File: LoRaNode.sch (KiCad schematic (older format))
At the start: 60 parts, among them J1 CONN_01X04, J10 D4, J11 A1, J12 A2, J13 A3, J14 D8, J2 Conn_01x06, J3 Conn_01x02, J4 ISP, J5 Conn_01x06, J6 Conn_01x04, J7 USB_B_Micro, J8 D2, J9 D3, U1 RFM95W-868S2, U2 MCP73871, U3 TPS63031, U4 ATMEGA328P-AU, Y1 8MHz HC5032/4

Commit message: v0.1
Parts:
- removed C10, C4, C5, C6, C7, C9: 10u, Capacitors_SMD:C_0805, symbol device:C
- removed C3: 4700uF/10V, Capacitors_THT:CP_Radial_D12.5mm_P25mm, symbol device:CP
- removed C8: 100n, Capacitors_SMD:C_0603, symbol device:C
- removed D1: MBR120VLSFT1G, Capacitors_SMD:C_0805, symbol device:D
- removed D2: CHRG, LEDs:LED_0805, symbol device:LED
- removed D3: DONE, LEDs:LED_0805, symbol device:LED
- removed D4: PWR, LEDs:LED_0805, symbol device:LED
- removed J1: CONN_01X04, Mlab_CON:RJ12GLP-AMP(RJ12), symbol LoRaNode-rescue:CONN_01X04-RESCUE-Arduino_Mini-Arduino_Mini-rescue
- removed J2: Conn_01x06, Pin_Headers:Pin_Header_Straight_1x06_Pitch2.54mm, symbol Connector:Conn_01x06
- removed J3: Conn_01x02, Pin_Headers:Pin_Header_Straight_1x02_Pitch2.54mm, symbol Connector:Conn_01x02
- removed J7: USB_B_Micro, Connector_USB:USB_Micro-B_Molex-105017-0001, symbol Connector:USB_B_Micro
- removed L2: 1u5, Inductors:Inductor_Wurth_MAPI-3012, symbol device:L
- removed R1, R2, R3: 1k, Resistors_SMD:R_0603, symbol device:R
- removed R10: 69k8, Resistors_SMD:R_0603, symbol device:R
- removed R4: 270k, Resistors_SMD:R_0603, symbol device:R
- removed R5, R7: 100k, Resistors_SMD:R_0603, symbol device:R
- removed R6: 2k, Resistors_SMD:R_0603, symbol device:R
- removed R8: 1k54, Resistors_SMD:R_0603, symbol device:R
- removed R9: THERM 10k, Resistors_SMD:R_0805, symbol device:R
- removed U2: MCP73871, Housings_DFN_QFN:QFN-20-1EP_4x4mm_Pitch0.5mm, symbol MLAB_IO:MCP73871
- removed U3: TPS63031, Package_SON:Texas_S-PWSON-N10, symbol MLAB_IO:TPS63031
- added J1: A3, TestPoint:TestPoint_Pad_D1.0mm, symbol Connector:Conn_01x01
- added J2: Conn_01x03, Connector_PinHeader_2.54mm:PinHeader_1x03_P2.54mm_Vertical, symbol Connector:Conn_01x03
- C1: value 2p7 -> dnp
- L1: value 1n8 -> 0R
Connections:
- net labels added: GND
- net labels removed: A4, A5, Earth, VOUT, VSOL
- wire segments 223 -> 110
- no-connect marks 9 -> 6
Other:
- note added: "LoRa Node"
- note removed: "Charge Rate = 1000V/PROG1\n1k = 1000 mA\n2k = 500 mA"
- note removed: "No Thermistor: RT1 = 0R, RT2 = 10k\n10k NTC Thermistor: RT1 = 1k54, RT2 = 69k8"
- note removed: "ToDo:\nChange ground symbols\n"
- moved on the sheet: C1, C11, C12, C13, C14, C15, C16, C17, C18, C19, C2, C20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

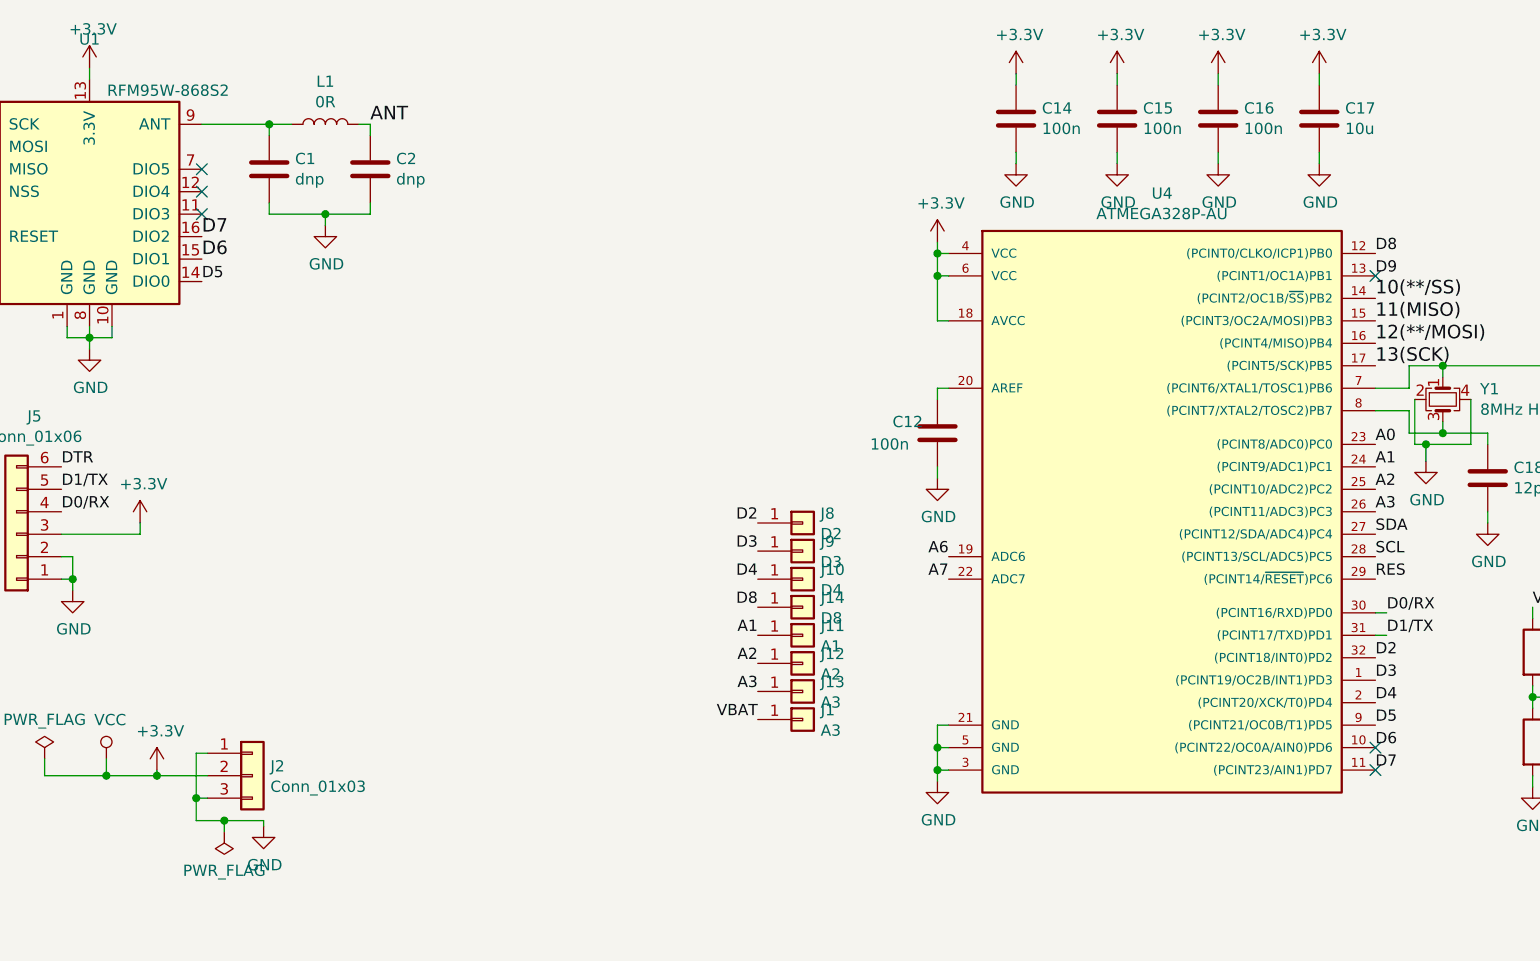
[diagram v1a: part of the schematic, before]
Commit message: Moved I2C and Power connectors, Added antenna test pads, ERC done, DRC done
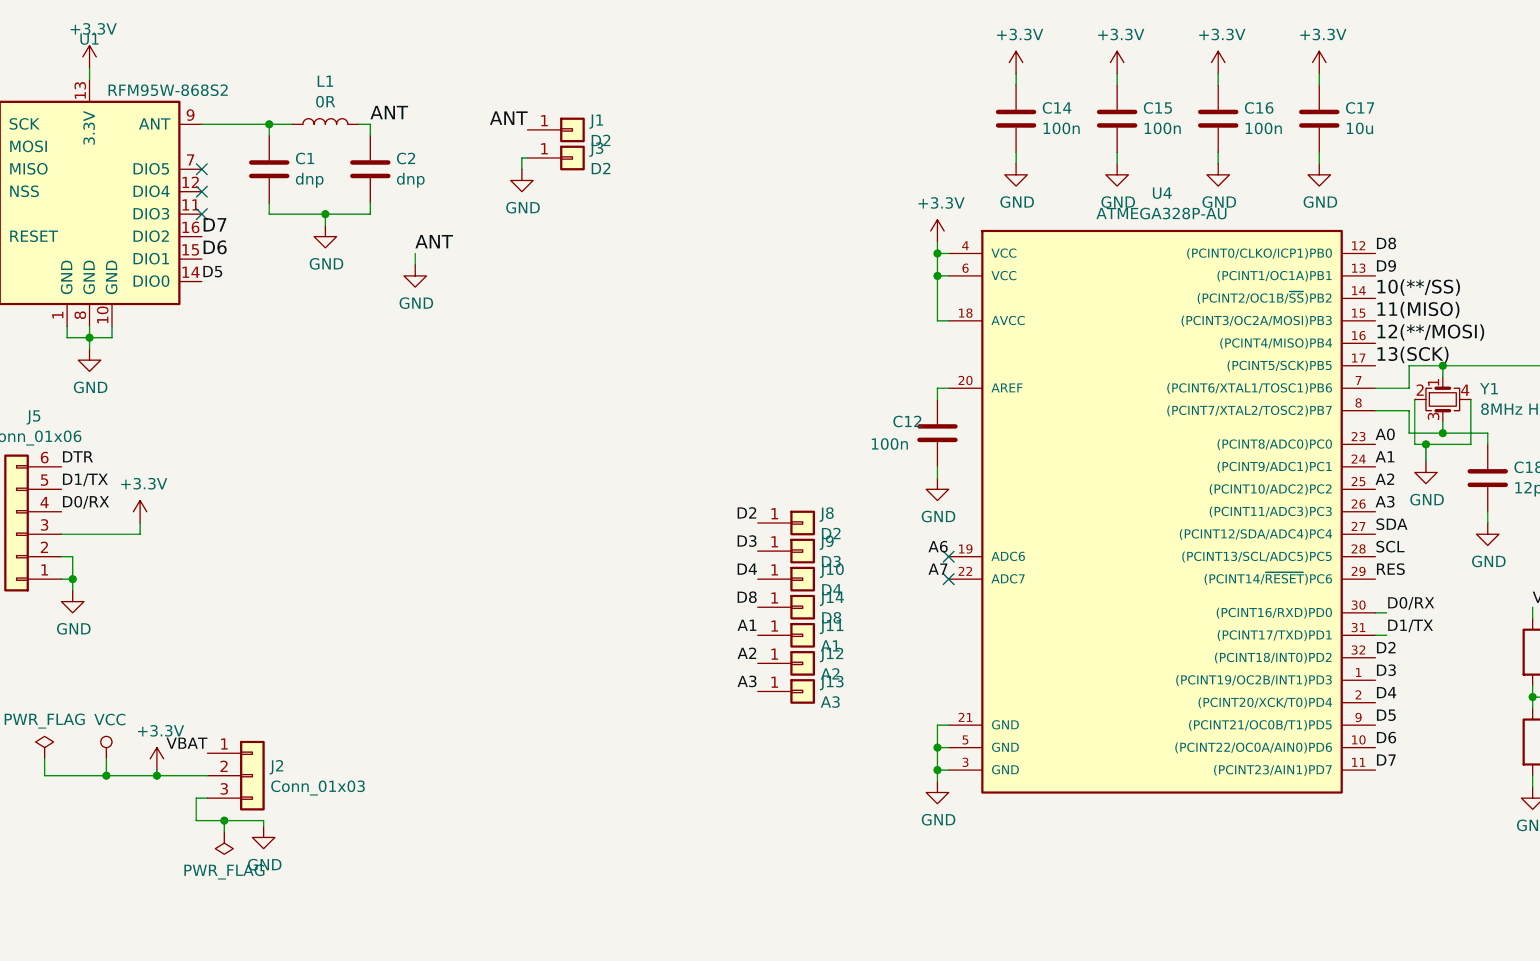
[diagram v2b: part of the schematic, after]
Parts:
- added J3: D2, TestPoint:TestPoint_Pad_1.0x1.0mm, symbol Connector:Conn_01x01
- J1: value A3 -> D2; footprint TestPoint:TestPoint_Pad_D1.0mm -> TestPoint:TestPoint_Pad_2.0x2.0mm
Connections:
- wire segments 110 -> 111
- no-connect marks 6 -> 5
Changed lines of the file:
@@
 Text Label 3775 3100 0    50   ~ 0
 D5
-NoConn ~ 9000 5175
-NoConn ~ 9000 5275
-NoConn ~ 9000 3075
 $Comp
 L device:R R16
@@
 	4050 5500 4050 5525
 Wire Wire Line
-	3800 5200 3750 5200
-Wire Wire Line
-	3750 5200 3750 5400
-Wire Wire Line
 	3750 5500 3875 5500
 Wire Wire Line
 	3800 5400 3750 5400
-Connection ~ 3750 5400
 Wire Wire Line
 	3750 5400 3750 5500
@@
 	1    0    0    -1
 $EndComp
+Text Label 3800 5200 2    50   ~ 0
+VBAT
 $Comp
 L Connector:Conn_01x01 J1
-U 1 1 5C90461F
-P 6450 5050
-F 0 "J1" H 6530 5092 50  0000 L CNN
-F 1 "A3" H 6530 5001 50  0000 L CNN
-F 2 "TestPoint:TestPoint_Pad_D1.0mm" H 6450 5050 50  0001 C CNN
-F 3 "~" H 6450 5050 50  0001 C CNN
-	1    6450 5050
-	1    0    0    -1
-$EndComp
-Text Label 6250 5050 2    50   ~ 0
-VBAT
+U 1 1 5C94DB3B
+P 5425 2425
+F 0 "J1" H 5504 2467 50  0000 L CNN
+F 1 "D2" H 5504 2376 50  0000 L CNN
+F 2 "TestPoint:TestPoint_Pad_2.0x2.0mm" H 5425 2425 50  0001 C CNN
+F 3 "~" H 5425 2425 50  0001 C CNN
+	1    5425 2425
+	1    0    0    -1
+$EndComp
+Text Label 5225 2425 2    60   ~ 0
+ANT
+$Comp
+L Connector:Conn_01x01 J3
+U 1 1 5C9511AC
+P 5425 2550
+F 0 "J3" H 5504 2592 50  0000 L CNN
+F 1 "D2" H 5504 2501 50  0000 L CNN
+F 2 "TestPoint:TestPoint_Pad_1.0x1.0mm" H 5425 2550 50  0001 C CNN
+F 3 "~" H 5425 2550 50  0001 C CNN
+	1    5425 2550
+	1    0    0    -1
+$EndComp
+$Comp
+L power:GND #PWR0121
+U 1 1 5C95121C
+P 5200 2600
+F 0 "#PWR0121" H 5200 2350 50  0001 C CNN
+F 1 "GND" H 5205 2427 50  0000 C CNN
+F 2 "" H 5200 2600 50  0001 C CNN
+F 3 "" H 5200 2600 50  0001 C CNN
+	1    5200 2600
+	1    0    0    -1
+$EndComp
+Wire Wire Line
+	5225 2550 5200 2550
+Wire Wire Line
+	5200 2550 5200 2600
+NoConn ~ 7100 4325
+NoConn ~ 7100 4425
+Text Label 4725 2975 0    60   ~ 0
+ANT
+$Comp
+L power:GND #PWR0122
+U 1 1 5C95F96A
+P 4725 3025
+F 0 "#PWR0122" H 4725 2775 50  0001 C CNN
+F 1 "GND" H 4730 2852 50  0000 C CNN
+F 2 "" H 4725 3025 50  0001 C CNN
+F 3 "" H 4725 3025 50  0001 C CNN
+	1    4725 3025
+	1    0    0    -1
+$EndComp
+Wire Wire Line
+	4725 2975 4725 3025
 $EndSCHEMATC

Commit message: Changed I2C pinout
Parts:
- added J7: A3, TestPoint:TestPoint_Pad_D1.0mm, symbol Connector:Conn_01x01
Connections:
- no-connect marks 5 -> 4
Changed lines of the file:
@@
 	-1   0    0    1
 $EndComp
+Text Label 1875 5450 0    50   ~ 0
+SDA
 Text Label 1875 5350 0    50   ~ 0
-SDA
-Text Label 1875 5450 0    50   ~ 0
 SCL
 $Comp
@@
 	5200 2550 5200 2600
 NoConn ~ 7100 4325
-NoConn ~ 7100 4425
 Text Label 4725 2975 0    60   ~ 0
 ANT
@@
 Wire Wire Line
 	4725 2975 4725 3025
+$Comp
+L Connector:Conn_01x01 J7
+U 1 1 5C9520C6
+P 6450 5050
+F 0 "J7" H 6530 5092 50  0000 L CNN
+F 1 "A3" H 6530 5001 50  0000 L CNN
+F 2 "TestPoint:TestPoint_Pad_D1.0mm" H 6450 5050 50  0001 C CNN
+F 3 "~" H 6450 5050 50  0001 C CNN
+	1    6450 5050
+	1    0    0    -1
+$EndComp
+Text Label 6250 5050 2    50   ~ 0
+A7
 $EndSCHEMATC

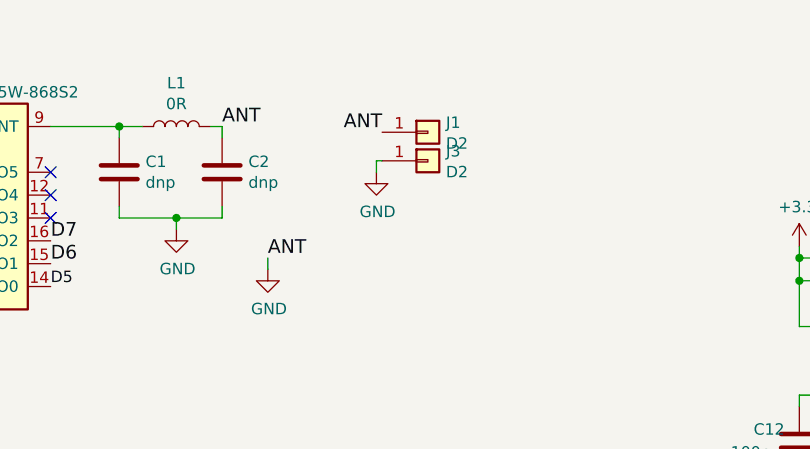
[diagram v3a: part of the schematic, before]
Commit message: Silkscreen correction, removed antenna testing pads
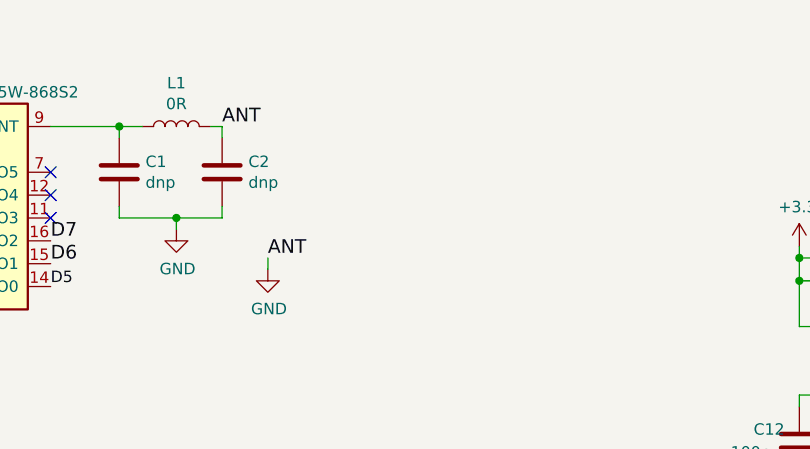
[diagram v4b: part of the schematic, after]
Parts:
- removed J1: D2, TestPoint:TestPoint_Pad_2.0x2.0mm, symbol Connector:Conn_01x01
- removed J3: D2, TestPoint:TestPoint_Pad_1.0x1.0mm, symbol Connector:Conn_01x01
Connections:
- wire segments 111 -> 109
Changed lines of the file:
@@
 Text Label 3800 5200 2    50   ~ 0
 VBAT
-$Comp
-L Connector:Conn_01x01 J1
-U 1 1 5C94DB3B
-P 5425 2425
-F 0 "J1" H 5504 2467 50  0000 L CNN
-F 1 "D2" H 5504 2376 50  0000 L CNN
-F 2 "TestPoint:TestPoint_Pad_2.0x2.0mm" H 5425 2425 50  0001 C CNN
-F 3 "~" H 5425 2425 50  0001 C CNN
-	1    5425 2425
-	1    0    0    -1
-$EndComp
-Text Label 5225 2425 2    60   ~ 0
-ANT
-$Comp
-L Connector:Conn_01x01 J3
-U 1 1 5C9511AC
-P 5425 2550
-F 0 "J3" H 5504 2592 50  0000 L CNN
-F 1 "D2" H 5504 2501 50  0000 L CNN
-F 2 "TestPoint:TestPoint_Pad_1.0x1.0mm" H 5425 2550 50  0001 C CNN
-F 3 "~" H 5425 2550 50  0001 C CNN
-	1    5425 2550
-	1    0    0    -1
-$EndComp
-$Comp
-L power:GND #PWR0121
-U 1 1 5C95121C
-P 5200 2600
-F 0 "#PWR0121" H 5200 2350 50  0001 C CNN
-F 1 "GND" H 5205 2427 50  0000 C CNN
-F 2 "" H 5200 2600 50  0001 C CNN
-F 3 "" H 5200 2600 50  0001 C CNN
-	1    5200 2600
-	1    0    0    -1
-$EndComp
-Wire Wire Line
-	5225 2550 5200 2550
-Wire Wire Line
-	5200 2550 5200 2600
 NoConn ~ 7100 4325
-Text Label 4725 2975 0    60   ~ 0
-ANT
-$Comp
-L power:GND #PWR0122
-U 1 1 5C95F96A
-P 4725 3025
-F 0 "#PWR0122" H 4725 2775 50  0001 C CNN
-F 1 "GND" H 4730 2852 50  0000 C CNN
-F 2 "" H 4725 3025 50  0001 C CNN
-F 3 "" H 4725 3025 50  0001 C CNN
-	1    4725 3025
-	1    0    0    -1
-$EndComp
-Wire Wire Line
-	4725 2975 4725 3025
 $Comp
 L Connector:Conn_01x01 J7
@@
 Text Label 6250 5050 2    50   ~ 0
 A7
+Wire Wire Line
+	4725 2975 4725 3025
+$Comp
+L power:GND #PWR0122
+U 1 1 5C95F96A
+P 4725 3025
+F 0 "#PWR0122" H 4725 2775 50  0001 C CNN
+F 1 "GND" H 4730 2852 50  0000 C CNN
+F 2 "" H 4725 3025 50  0001 C CNN
+F 3 "" H 4725 3025 50  0001 C CNN
+	1    4725 3025
+	1    0    0    -1
+$EndComp
+Text Label 4725 2975 0    60   ~ 0
+ANT
 $EndSCHEMATC

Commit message: Added more 5 GPIO's and push button
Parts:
- removed J11: A1, TestPoint:TestPoint_Pad_D1.0mm, symbol Connector:Conn_01x01
- removed J12: A2, TestPoint:TestPoint_Pad_D1.0mm, symbol Connector:Conn_01x01
- removed J13, J7: A3, TestPoint:TestPoint_Pad_D1.0mm, symbol Connector:Conn_01x01
- removed J14: D8, TestPoint:TestPoint_Pad_D1.0mm, symbol Connector:Conn_01x01
- removed J6: Conn_01x04, Pin_Headers:Pin_Header_Straight_1x04_Pitch2.54mm, symbol Connector:Conn_01x04
- added J1: Conn_01x09, Connector_PinSocket_2.54mm:PinSocket_1x09_P2.54mm_Vertical, symbol Connector:Conn_01x09
- added R1: 100k, Resistor_SMD:R_0603_1608Metric, symbol device:R
- added SW1: SW_Push, kicad-footprints-master:SMD-PushButton-6x3.6mm, symbol Switch:SW_Push
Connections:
- wire segments 109 -> 113
- no-connect marks 4 -> 3
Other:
- moved on the sheet: C12, C14, C15, C16, C17, C18, C19, C20, J10, J2, J4, J5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
